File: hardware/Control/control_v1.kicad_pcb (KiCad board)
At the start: 2 copper layers, 29 parts, among them J1 Conn_02x07_Counter_Clockwise, J2 Screw_Terminal_01x05, J3 Conn_01x06, J4 RJ45, M1 STM32F4-DISCOVERY, U1 TL2575HV-ADJ, U2 TL2575HV-ADJ

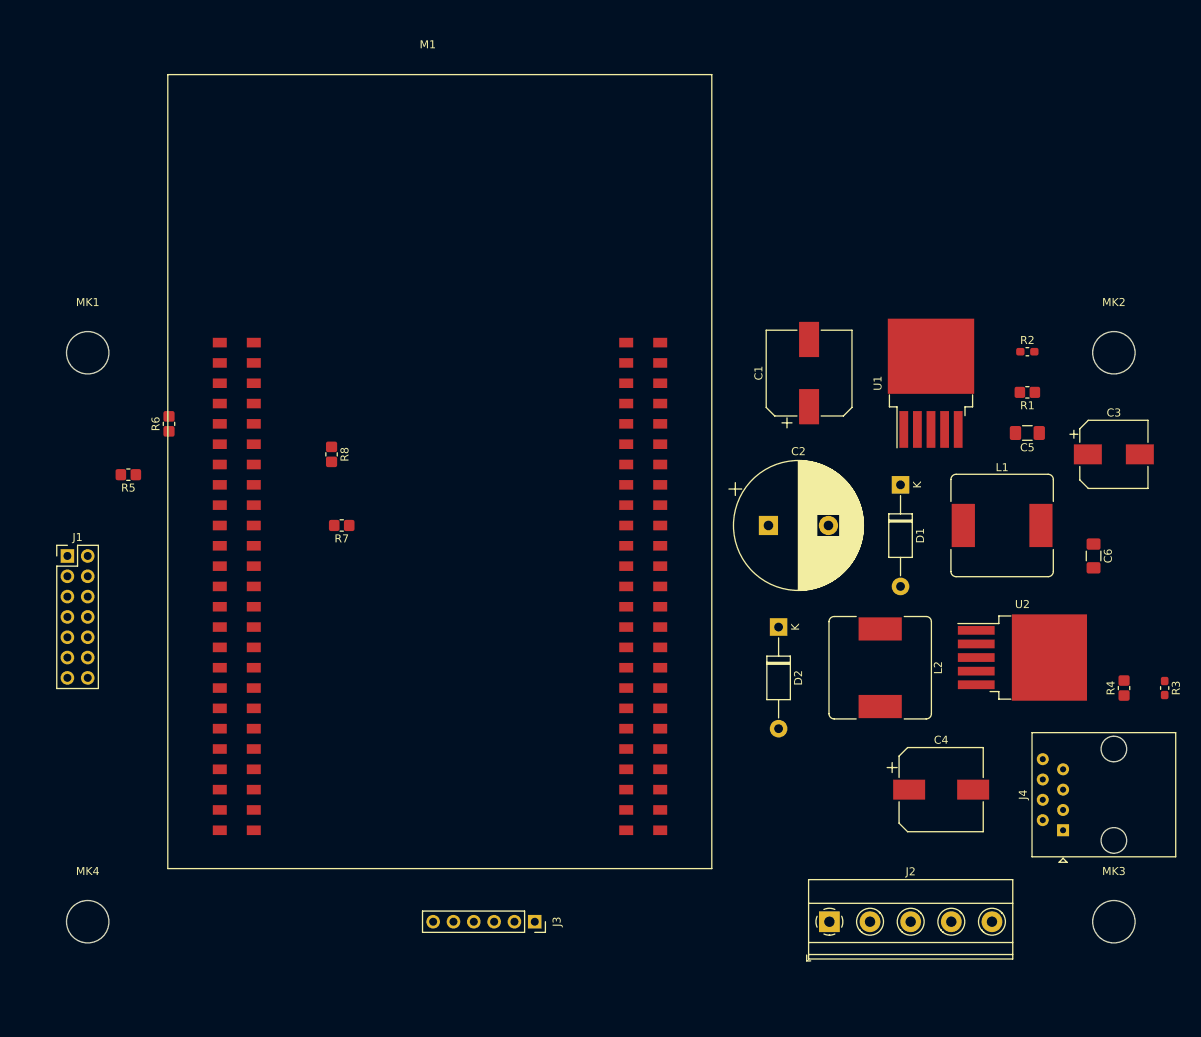
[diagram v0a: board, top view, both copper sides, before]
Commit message: Added filter components and baord layout
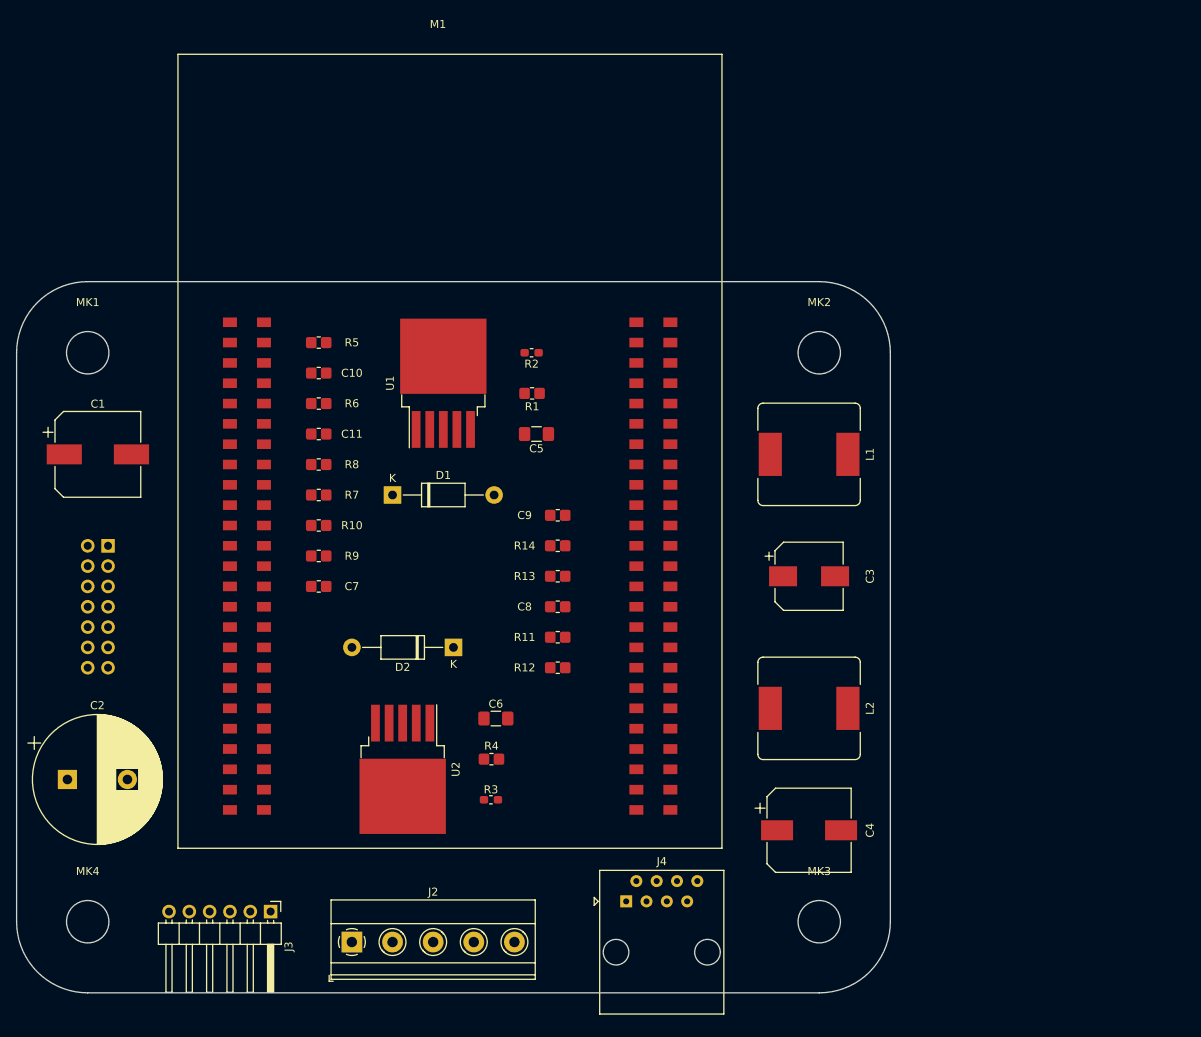
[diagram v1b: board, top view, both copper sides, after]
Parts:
- added C10: 2.2nF, Capacitor_SMD:C_0805_2012Metric_Pad1.33x1.40mm_HandSolder, F.Cu at (143.2, 68.6)
- added C11: 2.2nF, Capacitor_SMD:C_0805_2012Metric_Pad1.33x1.40mm_HandSolder, F.Cu at (143.2, 76.2)
- added C7: 2.2nF, Capacitor_SMD:C_0805_2012Metric_Pad1.33x1.40mm_HandSolder, F.Cu at (143.2, 95.2)
- added C8: 2.2nF, Capacitor_SMD:C_0805_2012Metric_Pad1.33x1.40mm_HandSolder, F.Cu at (173.1, 97.8)
- added C9: 2.2nF, Capacitor_SMD:C_0805_2012Metric_Pad1.33x1.40mm_HandSolder, F.Cu at (173.1, 86.4)
- added R10: 30k, Resistor_SMD:R_0805_2012Metric_Pad1.33x1.40mm_HandSolder, F.Cu at (143.2, 87.6)
- added R11: 18k, Resistor_SMD:R_0805_2012Metric_Pad1.33x1.40mm_HandSolder, F.Cu at (173.1, 101.6)
- added R12: 30k, Resistor_SMD:R_0805_2012Metric_Pad1.33x1.40mm_HandSolder, F.Cu at (173.1, 105.4)
- added R13: 18k, Resistor_SMD:R_0805_2012Metric_Pad1.33x1.40mm_HandSolder, F.Cu at (173.1, 94.0)
- added R14: 30k, Resistor_SMD:R_0805_2012Metric_Pad1.33x1.40mm_HandSolder, F.Cu at (173.1, 90.2)
- added R9: 18k, Resistor_SMD:R_0805_2012Metric_Pad1.33x1.40mm_HandSolder, F.Cu at (143.2, 91.4)
- J1: moved to B.Cu
- J3: footprint Connector_PinSocket_2.54mm:PinSocket_1x06_P2.54mm_Vertical -> Connector_PinHeader_2.54mm:PinHeader_1x06_P2.54mm_Horizontal
- moved C2 93.2 mm to (111.8, 119.4)
- moved C1 89.5 mm to (115.6, 78.7), turned to 0 degrees
- moved R3 85.4 mm to (164.7, 121.9), turned to 180 degrees
- moved R4 79.6 mm to (164.8, 116.8), turned to 0 degrees
- moved U2 78.7 mm to (153.7, 118.1), turned to 270 degrees
- moved C6 77.4 mm to (165.3, 111.8), turned to 0 degrees
- moved D1 63.5 mm to (152.4, 83.8), turned to 0 degrees
- moved R2 62.0 mm to (169.8, 66.0)
- moved R1 61.9 mm to (169.8, 71.1)
- moved C5 61.4 mm to (170.4, 76.2)
- moved U1 61.0 mm to (158.8, 69.8)
- moved J2 59.7 mm to (147.3, 139.7)
- moved J4 55.3 mm to (181.6, 134.6), turned to 0 degrees
- moved C3 41.0 mm to (204.5, 94.0)
- moved D2 40.7 mm to (160.0, 102.9), turned to 180 degrees
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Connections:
- M1 pad 22: /HALL_C -> /microcontroller/HALL_C_SENSE
- M1 pad 75: /HALL_A -> /microcontroller/HALL_A_SENSE
- M1 pad 76: /HALL_B -> /microcontroller/HALL_B_SENSE
- R5 pad 1: /microcontroller/PC5 -> /PHASEB_FB
- R5 pad 2: /PHASEB_FB -> /microcontroller/PC5
- R7 pad 1: /GND -> /microcontroller/PC4
- R7 pad 2: /microcontroller/PC4 -> /GND
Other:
- board outline added: 109.2 x 88.9 mm

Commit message: Laid all traces, updated documentation
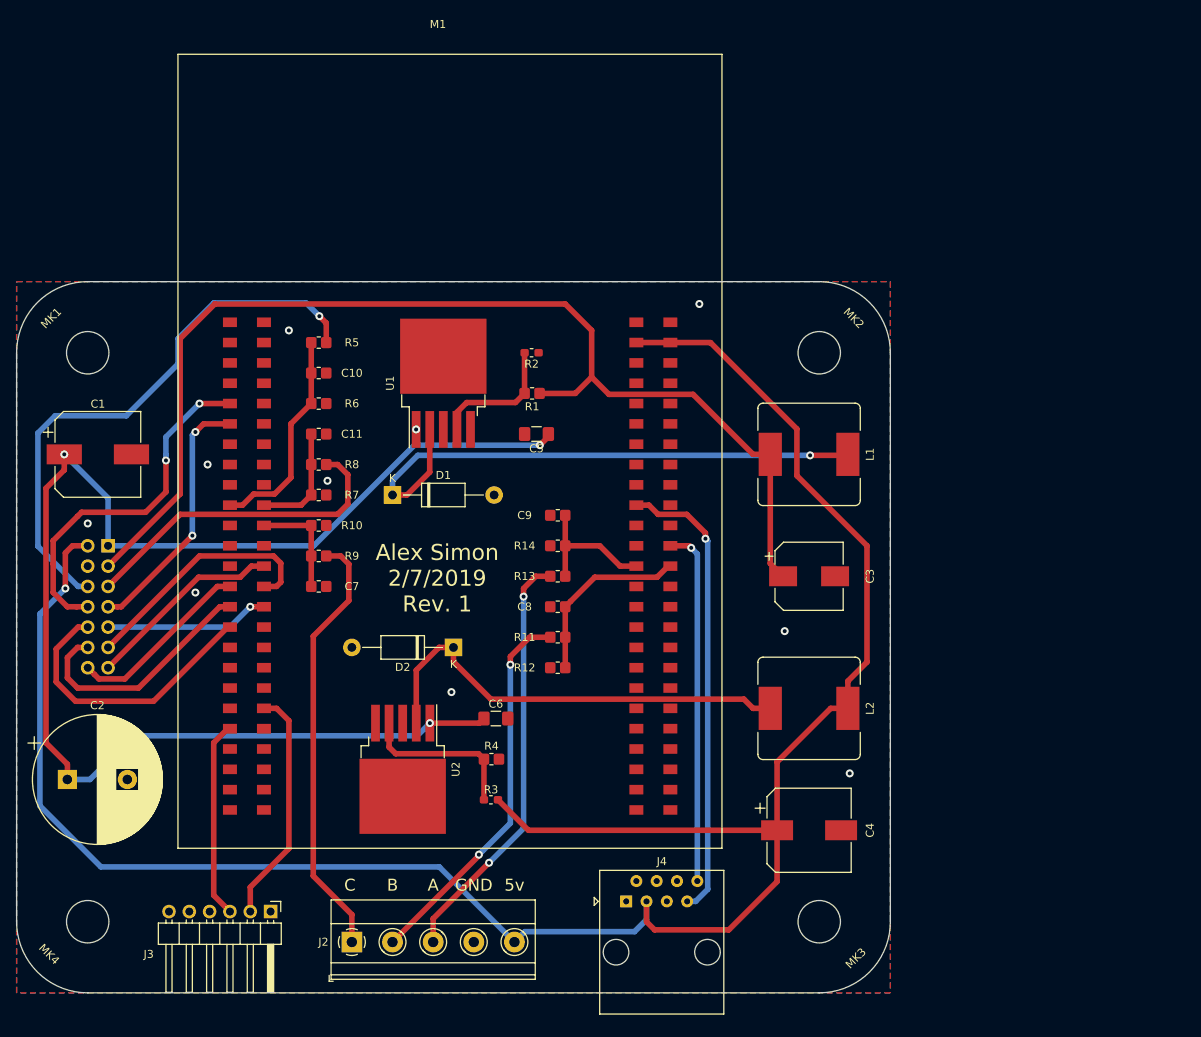
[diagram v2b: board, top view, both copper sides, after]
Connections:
- M1 pad 3: /3v -> Net-(M1-Pad3)
- M1 pad 4: /3v -> Net-(M1-Pad4)
- M1 pad 55: /3v -> Net-(M1-Pad55)
- M1 pad 56: /3v -> Net-(M1-Pad56)
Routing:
- net /5v: track 0.00 -> 271.3 mm, vias 0 -> 1
- net /48v: track 0.00 -> 174.6 mm, vias 0 -> 4
- net /12v: track 0.00 -> 142.2 mm
- net /powerconverters/12v_OUT: track 0.00 -> 71.3 mm, vias 0 -> 1
- net /PHASEB_FB: track 0.00 -> 70.6 mm, vias 0 -> 1
- net /I2C_SCL: track 0.00 -> 57.9 mm, vias 0 -> 1
- net /powerconverters/5v_OUT: track 0.00 -> 56.3 mm
- net /HALL_C: track 0.00 -> 54.3 mm
- net /HALL_A: track 0.00 -> 52.8 mm, vias 0 -> 2
- net /HALL_B: track 0.00 -> 47.8 mm, vias 0 -> 2
- net /AUX_1: track 0.00 -> 44.7 mm, vias 0 -> 2
- net /I2C_SDA: track 0.00 -> 44.7 mm, vias 0 -> 1
- net /PHASEA_FB: track 0.00 -> 41.1 mm
- net /HS_C_TTL_PWM: track 0.00 -> 35.7 mm
- net /AUX_0: track 0.00 -> 32.1 mm, vias 0 -> 2
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- added copper zone on B.Cu, net /GND
- added copper zone on F.Cu, net /GND
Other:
- net class Default: trace_width 0.5 -> 0.7
- board text added: "5v"
- board text added: "A"
- board text added: "Alex Simon 2/7/2019 Rev. 1"
- board text added: "B"
- board text added: "C"
- board text added: "GND"

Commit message: Added drill files
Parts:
- MK1, MK2, MK3, MK4: footprint MountingHole:MountingHole_5.3mm_M5 -> MountingHole:MountingHole_5.3mm_M5_DIN965_Pad
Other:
- board text added: "12v"
- board text added: "48v"
- board text added: "AFB"
- board text added: "AX0"
- board text added: "AX1"
- board text added: "BFB"
- board text added: "HAP"
- board text added: "HBP"
- board text added: "HCP"
- board text added: "LAP"
- board text added: "LBP"
- board text added: "LCP"
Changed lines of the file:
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@@
   (general
     (thickness 1.6)
-    (drawings 16)
+    (drawings 30)
     (tracks 263)
     (zones 0)
@@
     (mod_text_size 1 1)
     (mod_text_width 0.15)
-    (pad_size 1.524 1.524)
-    (pad_drill 0.762)
+    (pad_size 5.3 5.3)
+    (pad_drill 5.3)
     (pad_to_mask_clearance 0.2)
     (aux_axis_origin 0 0)
     (visible_elements FFFFFF7F)
     (pcbplotparams
-      (layerselection 0x010fc_ffffffff)
-      (usegerberextensions false)
+      (layerselection 0x010f0_ffffffff)
+      (usegerberextensions true)
       (usegerberattributes false)
       (usegerberadvancedattributes false)
@@
       (outputformat 1)
       (mirror false)
-      (drillshape 1)
+      (drillshape 0)
       (scaleselection 1)
-      (outputdirectory ""))
+      (outputdirectory "Gerber/"))
   )
   (net 0 "")
@@
       (net 2 /GND))
   )
-  (module MountingHole:MountingHole_5.3mm_M5 (layer F.Cu)
-    (at 114.3 66.04)
-    (descr "Mounting Hole 5.3mm, no annular, M5")
-    (tags "mounting hole 5.3mm no annular m5")
-    (attr virtual)
-    (fp_text reference MK1 (at -4.572 -4.318 225) (layer F.SilkS)
-      (effects (font (size 1 1) (thickness 0.15)))
-    )
-    (fp_text value Mounting_Hole (at 0 6.3) (layer F.Fab)
-      (effects (font (size 1 1) (thickness 0.15)))
-    )
-    (fp_circle (center 0 0) (end 5.55 0) (layer F.CrtYd) (width 0.05))
-    (fp_circle (center 0 0) (end 5.3 0) (layer Cmts.User) (width 0.15))
-    (fp_text user %R (at 0.3 0) (layer F.Fab)
-      (effects (font (size 1 1) (thickness 0.15)))
-    )
-    (pad 1 np_thru_hole circle (at 0 0) (size 5.3 5.3) (drill 5.3) (layers *.Cu *.Mask))
-  )
-  (module MountingHole:MountingHole_5.3mm_M5 (layer F.Cu)
-    (at 205.74 66.04)
-    (descr "Mounting Hole 5.3mm, no annular, M5")
-    (tags "mounting hole 5.3mm no annular m5")
-    (attr virtual)
-    (fp_text reference MK2 (at 4.318 -4.318 135) (layer F.SilkS)
-      (effects (font (size 1 1) (thickness 0.15)))
-    )
-    (fp_text value Mounting_Hole (at 0 6.3) (layer F.Fab)
-      (effects (font (size 1 1) (thickness 0.15)))
-    )
-    (fp_circle (center 0 0) (end 5.55 0) (layer F.CrtYd) (width 0.05))
-    (fp_circle (center 0 0) (end 5.3 0) (layer Cmts.User) (width 0.15))
-    (fp_text user %R (at 0.3 0) (layer F.Fab)
-      (effects (font (size 1 1) (thickness 0.15)))
-    )
-    (pad 1 np_thru_hole circle (at 0 0) (size 5.3 5.3) (drill 5.3) (layers *.Cu *.Mask))
-  )
-  (module MountingHole:MountingHole_5.3mm_M5 (layer F.Cu)
-    (at 205.74 137.16)
-    (descr "Mounting Hole 5.3mm, no annular, M5")
-    (tags "mounting hole 5.3mm no annular m5")
-    (attr virtual)
-    (fp_text reference MK3 (at 4.572 4.572 45) (layer F.SilkS)
-      (effects (font (size 1 1) (thickness 0.15)))
-    )
-    (fp_text value Mounting_Hole (at 0 6.3) (layer F.Fab)
-      (effects (font (size 1 1) (thickness 0.15)))
-    )
-    (fp_text user %R (at 0.3 0) (layer F.Fab)
-      (effects (font (size 1 1) (thickness 0.15)))
-    )
-    (fp_circle (center 0 0) (end 5.3 0) (layer Cmts.User) (width 0.15))
-    (fp_circle (center 0 0) (end 5.55 0) (layer F.CrtYd) (width 0.05))
-    (pad 1 np_thru_hole circle (at 0 0) (size 5.3 5.3) (drill 5.3) (layers *.Cu *.Mask))
-  )
-  (module MountingHole:MountingHole_5.3mm_M5 (layer F.Cu)
-    (at 114.3 137.16)
-    (descr "Mounting Hole 5.3mm, no annular, M5")
-    (tags "mounting hole 5.3mm no annular m5")
-    (attr virtual)
-    (fp_text reference MK4 (at -4.826 4.064 315) (layer F.SilkS)
-      (effects (font (size 1 1) (thickness 0.15)))
-    )
-    (fp_text value Mounting_Hole (at 0 6.3) (layer F.Fab)
-      (effects (font (size 1 1) (thickness 0.15)))
-    )
-    (fp_text user %R (at 0.3 0) (layer F.Fab)
-      (effects (font (size 1 1) (thickness 0.15)))
-    )
-    (fp_circle (center 0 0) (end 5.3 0) (layer Cmts.User) (width 0.15))
-    (fp_circle (center 0 0) (end 5.55 0) (layer F.CrtYd) (width 0.05))
-    (pad 1 np_thru_hole circle (at 0 0) (size 5.3 5.3) (drill 5.3) (layers *.Cu *.Mask))
-  )
   (module Resistor_SMD:R_0805_2012Metric_Pad1.33x1.40mm_HandSolder (layer F.Cu)
     (at 169.8475 71.12 180)
@@
     )
   )
+  (module MountingHole:MountingHole_5.3mm_M5_DIN965_Pad (layer F.Cu)
+    (at 114.3 66.04)
+    (descr "Mounting Hole 5.3mm, M5, DIN965")
+    (tags "mounting hole 5.3mm m5 din965")
+    (attr virtual)
+    (fp_text reference MK1 (at 0 -5.6) (layer F.SilkS)
+      (effects (font (size 1 1) (thickness 0.15)))
+    )
+    (fp_text value Mounting_Hole (at 0 5.6) (layer F.Fab)
+      (effects (font (size 1 1) (thickness 0.15)))
+    )
+    (fp_circle (center 0 0) (end 4.85 0) (layer F.CrtYd) (width 0.05))
+    (fp_circle (center 0 0) (end 4.6 0) (layer Cmts.User) (width 0.15))
+    (fp_text user %R (at 0.3 0) (layer F.Fab)
+      (effects (font (size 1 1) (thickness 0.15)))
+    )
+    (pad 1 thru_hole circle (at 0 0) (size 9.2 9.2) (drill 5.3) (layers *.Cu *.Mask))
+  )
+  (module MountingHole:MountingHole_5.3mm_M5_DIN965_Pad (layer F.Cu)
+    (at 205.74 66.04)
+    (descr "Mounting Hole 5.3mm, M5, DIN965")
+    (tags "mounting hole 5.3mm m5 din965")
+    (attr virtual)
+    (fp_text reference MK2 (at 0 -5.6) (layer F.SilkS)
+      (effects (font (size 1 1) (thickness 0.15)))
+    )
+    (fp_text value Mounting_Hole (at 0 5.6) (layer F.Fab)
+      (effects (font (size 1 1) (thickness 0.15)))
+    )
+    (fp_circle (center 0 0) (end 4.85 0) (layer F.CrtYd) (width 0.05))
+    (fp_circle (center 0 0) (end 4.6 0) (layer Cmts.User) (width 0.15))
+    (fp_text user %R (at 0.3 0) (layer F.Fab)
+      (effects (font (size 1 1) (thickness 0.15)))
+    )
+    (pad 1 thru_hole circle (at 0 0) (size 9.2 9.2) (drill 5.3) (layers *.Cu *.Mask))
+  )
+  (module MountingHole:MountingHole_5.3mm_M5_DIN965_Pad (layer F.Cu)
+    (at 205.74 137.16)
+    (descr "Mounting Hole 5.3mm, M5, DIN965")
+    (tags "mounting hole 5.3mm m5 din965")
+    (attr virtual)
+    (fp_text reference MK3 (at 0 6.096) (layer F.SilkS)
+      (effects (font (size 1 1) (thickness 0.15)))
+    )
+    (fp_text value Mounting_Hole (at 0 5.6) (layer F.Fab)
+      (effects (font (size 1 1) (thickness 0.15)))
+    )
+    (fp_text user %R (at 0.3 0) (layer F.Fab)
+      (effects (font (size 1 1) (thickness 0.15)))
+    )
+    (fp_circle (center 0 0) (end 4.6 0) (layer Cmts.User) (width 0.15))
+    (fp_circle (center 0 0) (end 4.85 0) (layer F.CrtYd) (width 0.05))
+    (pad 1 thru_hole circle (at 0 0) (size 9.2 9.2) (drill 5.3) (layers *.Cu *.Mask))
+  )
+  (module MountingHole:MountingHole_5.3mm_M5_DIN965_Pad (layer F.Cu)
+    (at 114.3 137.16)
+    (descr "Mounting Hole 5.3mm, M5, DIN965")
+    (tags "mounting hole 5.3mm m5 din965")
+    (attr virtual)
+    (fp_text reference MK4 (at 0 6.096) (layer F.SilkS)
+      (effects (font (size 1 1) (thickness 0.15)))
+    )
+    (fp_text value Mounting_Hole (at 0 5.6) (layer F.Fab)
+      (effects (font (size 1 1) (thickness 0.15)))
+    )
+    (fp_text user %R (at 0.3 0) (layer F.Fab)
+      (effects (font (size 1 1) (thickness 0.15)))
+    )
+    (fp_circle (center 0 0) (end 4.6 0) (layer Cmts.User) (width 0.15))
+    (fp_circle (center 0 0) (end 4.85 0) (layer F.CrtYd) (width 0.05))
+    (pad 1 thru_hole circle (at 0 0) (size 9.2 9.2) (drill 5.3) (layers *.Cu *.Mask))
+  )
+  (gr_text LAP (at 118.872 105.41) (layer F.SilkS)
+    (effects (font (size 1.5 1.5) (thickness 0.3)) (justify left))
+  )
+  (gr_text LBP (at 118.872 102.87) (layer F.SilkS)
+    (effects (font (size 1.5 1.5) (thickness 0.3)) (justify left))
+  )
+  (gr_text LCP (at 118.872 100.33) (layer F.SilkS)
+    (effects (font (size 1.5 1.5) (thickness 0.3)) (justify left))
+  )
+  (gr_text AX0 (at 119.126 97.79) (layer F.SilkS)
+    (effects (font (size 1.5 1.5) (thickness 0.3)) (justify left))
+  )
+  (gr_text AFB (at 119.126 95.25) (layer F.SilkS)
+    (effects (font (size 1.5 1.5) (thickness 0.3)) (justify left))
+  )
+  (gr_text 12v (at 119.126 92.71) (layer F.SilkS)
+    (effects (font (size 1.5 1.5) (thickness 0.3)) (justify left))
+  )
+  (gr_text 48v (at 119.126 90.17) (layer F.SilkS)
+    (effects (font (size 1.5 1.5) (thickness 0.3)) (justify left))
+  )
+  (gr_text HAP (at 112.268 105.41) (layer F.SilkS)
+    (effects (font (size 1.5 1.5) (thickness 0.3)) (justify right))
+  )
+  (gr_text HBP (at 112.268 102.87) (layer F.SilkS)
+    (effects (font (size 1.5 1.5) (thickness 0.3)) (justify right))
+  )
+  (gr_text HCP (at 112.268 100.33) (layer F.SilkS)
+    (effects (font (size 1.5 1.5) (thickness 0.3)) (justify right))
+  )
+  (gr_text AX1 (at 112.268 97.79) (layer F.SilkS)
+    (effects (font (size 1.5 1.5) (thickness 0.3)) (justify right))
+  )
+  (gr_text BFB (at 112.268 95.25) (layer F.SilkS)
+    (effects (font (size 1.5 1.5) (thickness 0.3)) (justify right))
+  )
+  (gr_text GND (at 112.268 92.71) (layer F.SilkS)
+    (effects (font (size 1.5 1.5) (thickness 0.3)) (justify right))
+  )
+  (gr_text 5v (at 112.268 90.17) (layer F.SilkS)
+    (effects (font (size 1.5 1.5) (thickness 0.3)) (justify right))
+  )
   (gr_circle (center 158.242 94.050189) (end 159.766 77.540189) (layer B.SilkS) (width 0.2))
